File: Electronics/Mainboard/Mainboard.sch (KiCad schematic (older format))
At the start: 6 parts, among them J1 609-5192-ND, J2 DB25_Male_MountingHoles, J3 609-5192-ND, J4 609-5192-ND, U14 LM75C

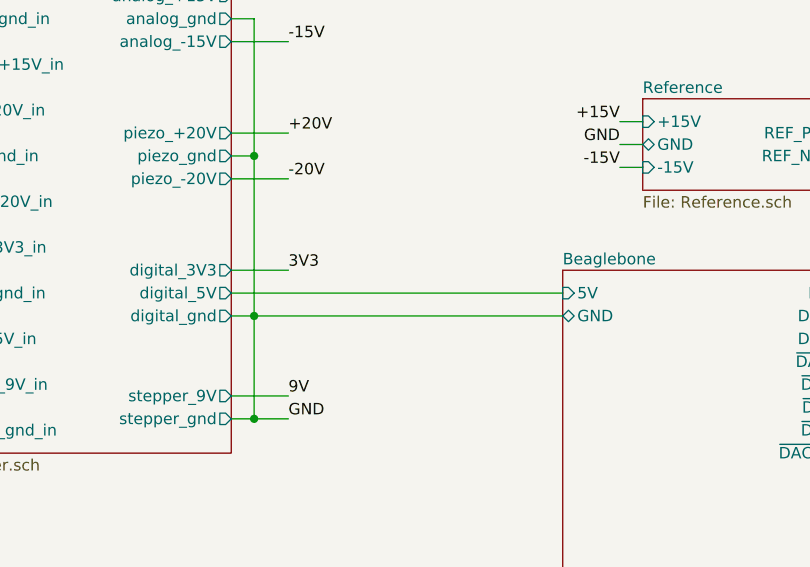
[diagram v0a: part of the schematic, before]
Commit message: Power supply routing progress
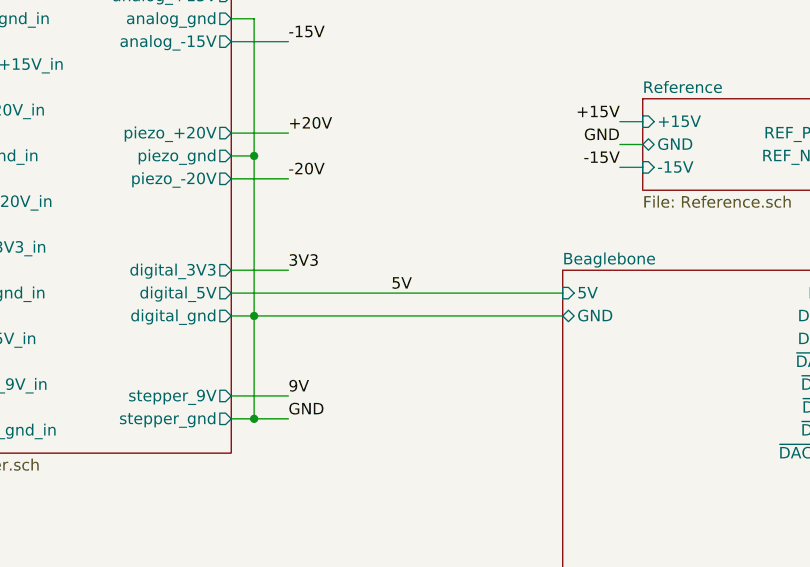
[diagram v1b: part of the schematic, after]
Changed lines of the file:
@@
 Wire Wire Line
 	6950 5500 7600 5500
+Text Label 4200 2600 0    50   ~ 0
+5V
 $EndSCHEMATC

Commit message: Layout nearly finished
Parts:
- added C138: 100n, Capacitor_SMD:C_0603_1608Metric_Pad1.05x0.95mm_HandSolder, symbol Device:C
- added JP11: Jumper_NC_Dual, Jumper:SolderJumper-3_P2.0mm_Open_TrianglePad1.0x1.5mm, symbol Device:Jumper_NC_Dual
- added R29: 4k7, Capacitor_SMD:C_0805_2012Metric_Pad1.15x1.40mm_HandSolder, symbol Device:R
- added TP11: TestPoint, TestPoint:TestPoint_Loop_D1.80mm_Drill1.0mm_Beaded, symbol Connector:TestPoint
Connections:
- net 3V3: now also U14.7 (A0), U14.8 (+Vs), C138.1, JP11.2, R29.2, TP11.1
- net GND: now also U14.4 (GND), U14.5 (A2), U14.6 (A1), C138.2
- net Shield: now reaches J2.0 (PAD)
- net i2c_scl: now reaches J2.12
- net i2c_scl: now also U14.2 (SCL)
- net i2c_sda: now reaches J2.13
- net i2c_sda: now also U14.1 (SDA), R29.1
- new net Beaglebone/3V3: JP11.1
- new net Power/digital_3V3: JP11.3
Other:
- note removed: "TODO: Analog Volotage on connector for preamp..."
- moved on the sheet: N1, U14
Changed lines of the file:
@@
 L Mechanical:Housing N1
 U 1 1 5D85575A
-P 15950 1700
-F 0 "N1" H 16103 1734 50  0000 L CNN
-F 1 "Housing" H 16103 1643 50  0000 L CNN
-F 2 "STM_Custom_Lib:Hammond_1455P1601" H 16000 1750 50  0001 C CNN
-F 3 "https://www.reichelt.de/profilgehaeuse-1455-p-160-x-120-x-30-5-mm-silber-1455p1601-p221381.html?&trstct=pol_6" H 16000 1750 50  0001 C CNN
-	1    15950 1700
+P 950 7250
+F 0 "N1" H 1103 7284 50  0000 L CNN
+F 1 "Housing" H 1103 7193 50  0000 L CNN
+F 2 "STM_Custom_Lib:Hammond_1455P1601" H 1000 7300 50  0001 C CNN
+F 3 "https://www.reichelt.de/profilgehaeuse-1455-p-160-x-120-x-30-5-mm-silber-1455p1601-p221381.html?&trstct=pol_6" H 1000 7300 50  0001 C CNN
+	1    950  7250
 	1    0    0    -1
 $EndComp
@@
 	1    0    0    -1
 $EndComp
-$Comp
-L Sensor_Temperature:LM75C U14
-U 1 1 5EB6D473
-P 14350 1800
-F 0 "U14" H 14350 2481 50  0000 C CNN
-F 1 "LM75C" H 14350 2390 50  0000 C CNN
-F 2 "Package_SO:SOIC-8_3.9x4.9mm_P1.27mm" H 14350 1800 50  0001 C CNN
-F 3 "http://www.ti.com/lit/ds/symlink/lm75b.pdf" H 14350 1800 50  0001 C CNN
-	1    14350 1800
-	1    0    0    -1
-$EndComp
-Wire Wire Line
-	14750 1800 14850 1800
-Wire Wire Line
-	14850 1800 14850 1900
-Wire Wire Line
-	14850 1900 14750 1900
-Wire Wire Line
-	14750 1700 14850 1700
+Wire Wire Line
+	5750 6600 5850 6600
+Wire Wire Line
+	5850 6600 5850 6700
+Wire Wire Line
+	5850 6700 5750 6700
+Wire Wire Line
+	5750 6500 5850 6500
 Wire Wire Line
 	10150 1150 10000 1150
@@
 F18 "Motor-Dir" O R 6400 5100 50
 F19 "Motor-Step" O R 6400 5000 50
+F20 "3V3" O L 4950 2800 50
+F21 "SDA" B L 4950 5000 50
+F22 "SCL" O L 4950 5100 50
 $EndSheet
 Wire Wire Line
@@
 	1    0    0    -1
 $EndComp
-Text Notes 13800 3350 0    71   ~ 0
-TODO: Analog Volotage on connector for preamp...
 Wire Wire Line
 	1750 1200 2150 1200
@@
 	3500 3050 3750 3050
 Wire Wire Line
-	3500 2500 3750 2500
-Wire Wire Line
 	3500 1900 3750 1900
 Wire Wire Line
@@
 Text Label 3750 3050 0    50   ~ 0
 9V
-Text Label 3750 2500 0    50   ~ 0
+Text Label 4450 2050 0    50   ~ 0
 3V3
 Text Label 3750 2100 0    50   ~ 0
@@
 Text Label 4200 2600 0    50   ~ 0
 5V
+$Comp
+L Device:Jumper_NC_Dual JP11
+U 1 1 5EFF93DD
+P 4350 2300
+F 0 "JP11" H 4350 2447 50  0001 C CNN
+F 1 "Jumper_NC_Dual" H 4350 2538 50  0001 C CNN
+F 2 "Jumper:SolderJumper-3_P2.0mm_Open_TrianglePad1.0x1.5mm" H 4350 2300 50  0001 C CNN
+F 3 "~" H 4350 2300 50  0001 C CNN
+	1    4350 2300
+	-1   0    0    1
+$EndComp
+Wire Wire Line
+	4450 2050 4350 2050
+Wire Wire Line
+	4350 2050 4350 2200
+Wire Wire Line
+	4600 2300 4750 2300
+Wire Wire Line
+	4750 2300 4750 2800
+Wire Wire Line
+	4750 2800 4950 2800
+Wire Wire Line
+	4100 2300 4000 2300
+Wire Wire Line
+	4000 2300 4000 2500
+Wire Wire Line
+	3500 2500 4000 2500
+$Comp
+L Connector:TestPoint TP?
+U 1 1 5F0439CF
+P 4400 1900
+AR Path="/5EE4ADA7/5F0439CF" Ref="TP?"  Part="1"
+AR Path="/5ED66353/5F0439CF" Ref="TP?"  Part="1"
+AR Path="/5F0439CF" Ref="TP11"  Part="1"
+F 0 "TP11" H 4458 2018 50  0001 L CNN
+F 1 "TestPoint" H 4458 1927 50  0001 L CNN
+F 2 "TestPoint:TestPoint_Loop_D1.80mm_Drill1.0mm_Beaded" H 4600 1900 50  0001 C CNN
+F 3 "~" H 4600 1900 50  0001 C CNN
+	1    4400 1900
+	0    1    1    0
+$EndComp
+Wire Wire Line
+	4400 1900 4350 1900
+Wire Wire Line
+	4350 1900 4350 2050
+Connection ~ 4350 2050
+Text Label 1350 900  1    50   ~ 0
+Shield
+Wire Wire Line
+	5350 7100 5350 7200
+Wire Wire Line
+	5850 6700 5850 7200
+Wire Wire Line
+	5850 7200 5350 7200
+Connection ~ 5850 6700
+Wire Wire Line
+	5850 6500 5850 6000
+Wire Wire Line
+	5850 6000 5350 6000
+Wire Wire Line
+	5350 6000 5350 6100
+Wire Wire Line
+	5850 6000 6050 6000
+Connection ~ 5850 6000
+Wire Wire Line
+	5850 7200 6050 7200
+Connection ~ 5850 7200
+Text Label 6150 7200 0    50   ~ 0
+GND
+Text Label 6150 6000 0    50   ~ 0
+3V3
+$Comp
+L Device:C C?
+U 1 1 5F13F70B
+P 6050 6600
+AR Path="/5D61E7C2/5DA22D82/5F13F70B" Ref="C?"  Part="1"
+AR Path="/5D61E7C2/5DAA3250/5F13F70B" Ref="C?"  Part="1"
+AR Path="/5D61E7C2/5DAA6516/5F13F70B" Ref="C?"  Part="1"
+AR Path="/5D61E7C2/5DAB2C4D/5F13F70B" Ref="C?"  Part="1"
+AR Path="/5D61E7C2/5EEC97A0/5F13F70B" Ref="C?"  Part="1"
+AR Path="/5D61E7C2/5ECB9506/5F13F70B" Ref="C?"  Part="1"
+AR Path="/5D61E7C2/5F13F70B" Ref="C?"  Part="1"
+AR Path="/5F13F70B" Ref="C138"  Part="1"
+F 0 "C138" V 6150 6650 50  0000 L CNN
+F 1 "100n" V 6150 6550 50  0000 R CNN
+F 2 "Capacitor_SMD:C_0603_1608Metric_Pad1.05x0.95mm_HandSolder" H 6088 6450 50  0001 C CNN
+F 3 "~" H 6050 6600 50  0001 C CNN
+	1    6050 6600
+	1    0    0    -1
+$EndComp
+Wire Wire Line
+	6050 6450 6050 6000
+Connection ~ 6050 6000
+Wire Wire Line
+	6050 6000 6150 6000
+Wire Wire Line
+	6050 6750 6050 7200
+Connection ~ 6050 7200
+Wire Wire Line
+	6050 7200 6150 7200
+$Comp
+L Device:R R?
+U 1 1 5F1B9FC8
+P 4600 4800
+AR Path="/5D61E7C2/5F1B9FC8" Ref="R?"  Part="1"
+AR Path="/5F1B9FC8" Ref="R29"  Part="1"
+F 0 "R29" V 4500 4700 50  0000 C CNN
+F 1 "4k7" V 4500 4900 50  0000 C CNN
+F 2 "Capacitor_SMD:C_0805_2012Metric_Pad1.15x1.40mm_HandSolder" V 4530 4800 50  0001 C CNN
+F 3 "~" H 4600 4800 50  0001 C CNN
+	1    4600 4800
+	0    1    1    0
+$EndComp
+Text Label 4350 5100 2    50   ~ 0
+i2c_scl
+Text Label 4350 5000 2    50   ~ 0
+i2c_sda
+Wire Wire Line
+	4350 5100 4950 5100
+Wire Wire Line
+	4950 5000 4800 5000
+Wire Wire Line
+	4750 4800 4800 4800
+Wire Wire Line
+	4800 4800 4800 5000
+Connection ~ 4800 5000
+Wire Wire Line
+	4800 5000 4350 5000
+Wire Wire Line
+	4450 4800 4350 4800
+Text Label 4350 4800 2    50   ~ 0
+3V3
+$Comp
+L Sensor_Temperature:LM75C U14
+U 1 1 5EB6D473
+P 5350 6600
+F 0 "U14" H 4850 6300 50  0000 C CNN
+F 1 "LM75C" H 4850 6200 50  0000 C CNN
+F 2 "Package_SO:SOIC-8_3.9x4.9mm_P1.27mm" H 5350 6600 50  0001 C CNN
+F 3 "http://www.ti.com/lit/ds/symlink/lm75b.pdf" H 5350 6600 50  0001 C CNN
+	1    5350 6600
+	1    0    0    -1
+$EndComp
+Text Label 4800 6600 2    50   ~ 0
+i2c_scl
+Text Label 4800 6500 2    50   ~ 0
+i2c_sda
+Wire Wire Line
+	4950 6500 4800 6500
+Wire Wire Line
+	4950 6600 4800 6600
+Text Label 1750 3400 0    50   ~ 0
+i2c_scl
+Text Label 1750 3600 0    50   ~ 0
+i2c_sda
 $EndSCHEMATC

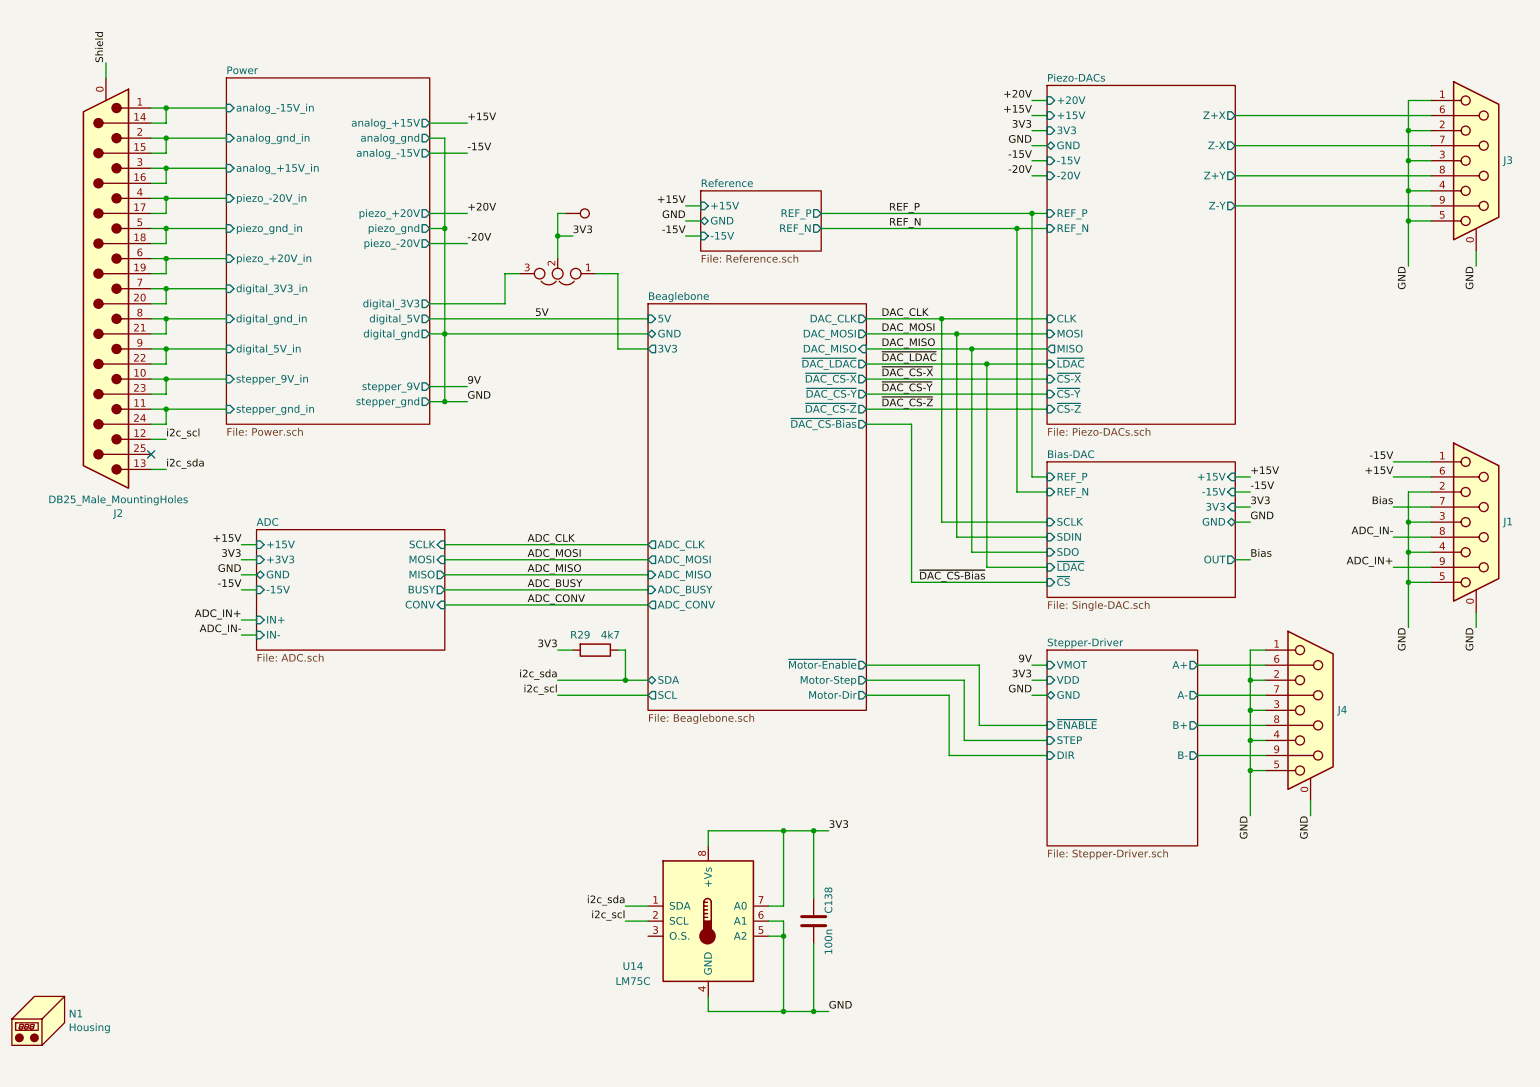
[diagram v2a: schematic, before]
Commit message: Silkscreen rearanged
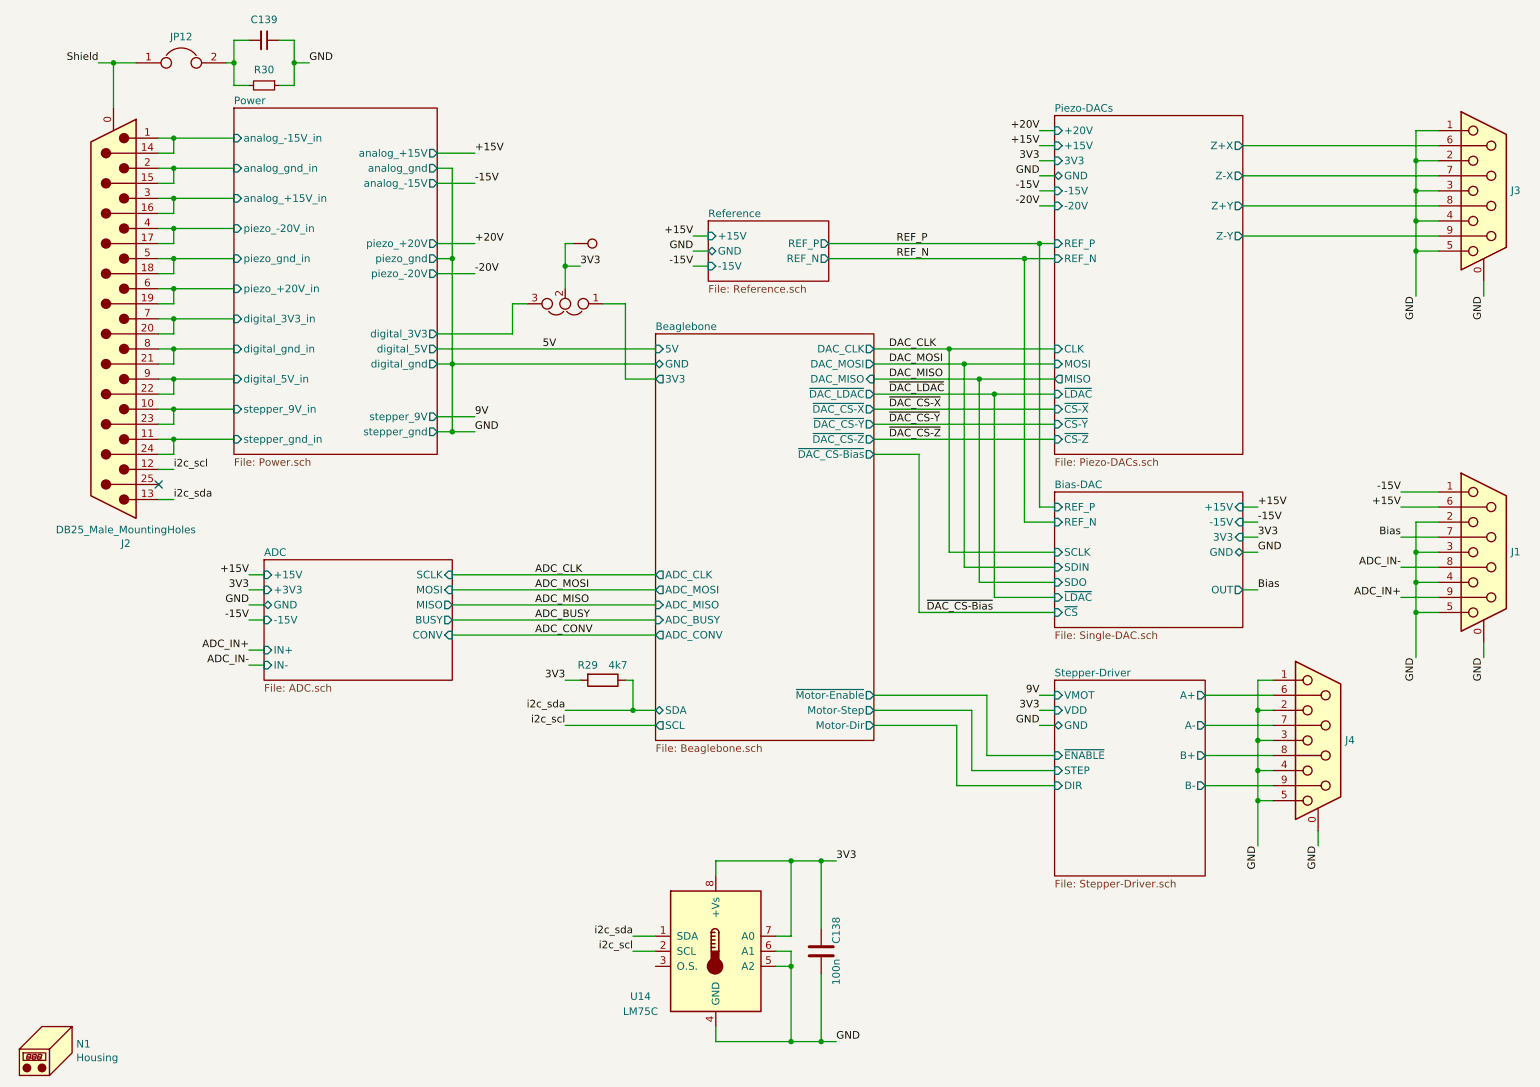
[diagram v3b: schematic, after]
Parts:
- added C139: C_Small, Capacitor_SMD:C_1206_3216Metric_Pad1.42x1.75mm_HandSolder, symbol Device:C_Small
- added JP12: Jumper, Jumper:SolderJumper-2_P1.3mm_Open_TrianglePad1.0x1.5mm, symbol Device:Jumper
- added R30: R_Small, Resistor_SMD:R_1206_3216Metric_Pad1.42x1.75mm_HandSolder, symbol Device:R_Small
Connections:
- net GND: now also C139.1, R30.1
- net Shield: now also JP12.1
- new net: C139.2, JP12.2, R30.2
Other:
- moved on the sheet: C138, J1, J2, J3, J4, N1, R29, U14
